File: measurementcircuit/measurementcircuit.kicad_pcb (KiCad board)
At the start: 2 copper layers, 27 parts, among them J1 2601-3110, J10 Conn_01x02, J11 Conn_01x02, J12 Conn_01x02, J2 2604-3106, J3 2604-3102, J4 2604-3102, J5 2604-3102, J6 2604-3102, J7 2604-3102, J8 Conn_01x02, J9 Conn_01x02

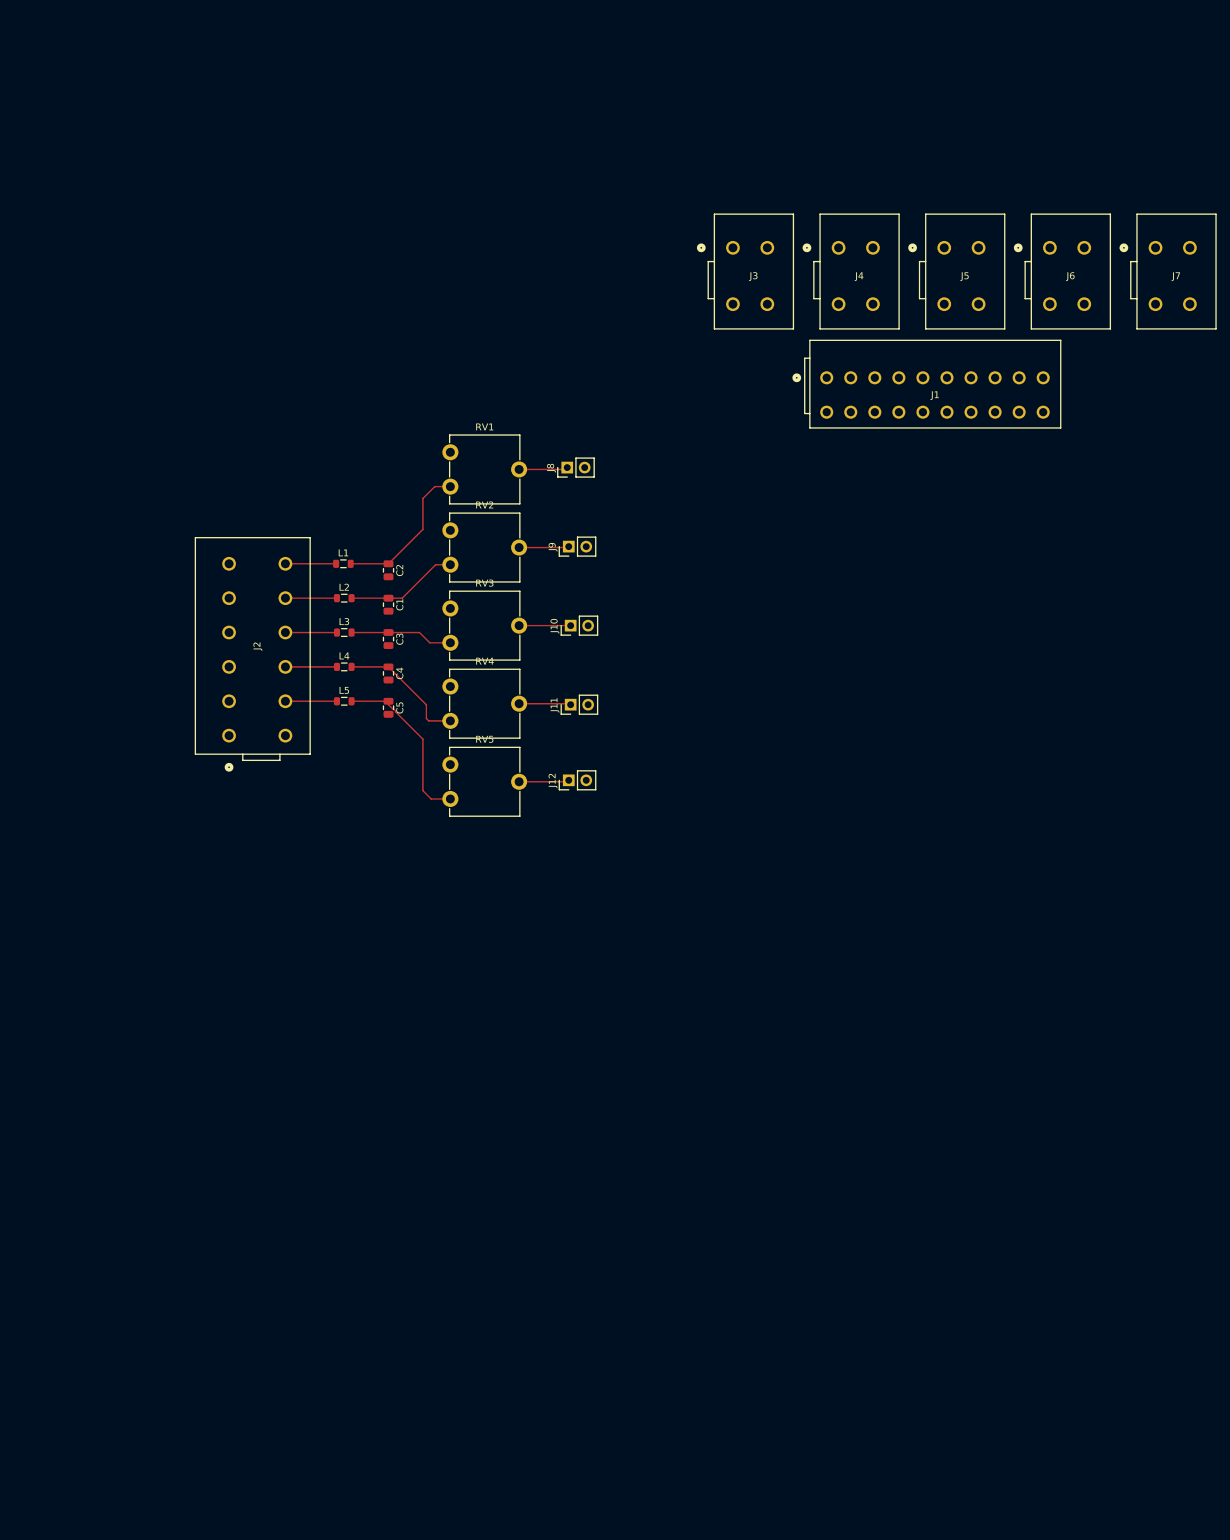
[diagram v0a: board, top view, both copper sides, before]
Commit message: Daniel Measurement Circuit Work
Add more routes to make a total of 8 circuits, component selections and placement, routing, finish schematic and pcb design. Switched back to 3 different circuits with shunts. Just need to fix some issues in the Design Rule Check (DRC) caused by the trace width increase aftor placing routes
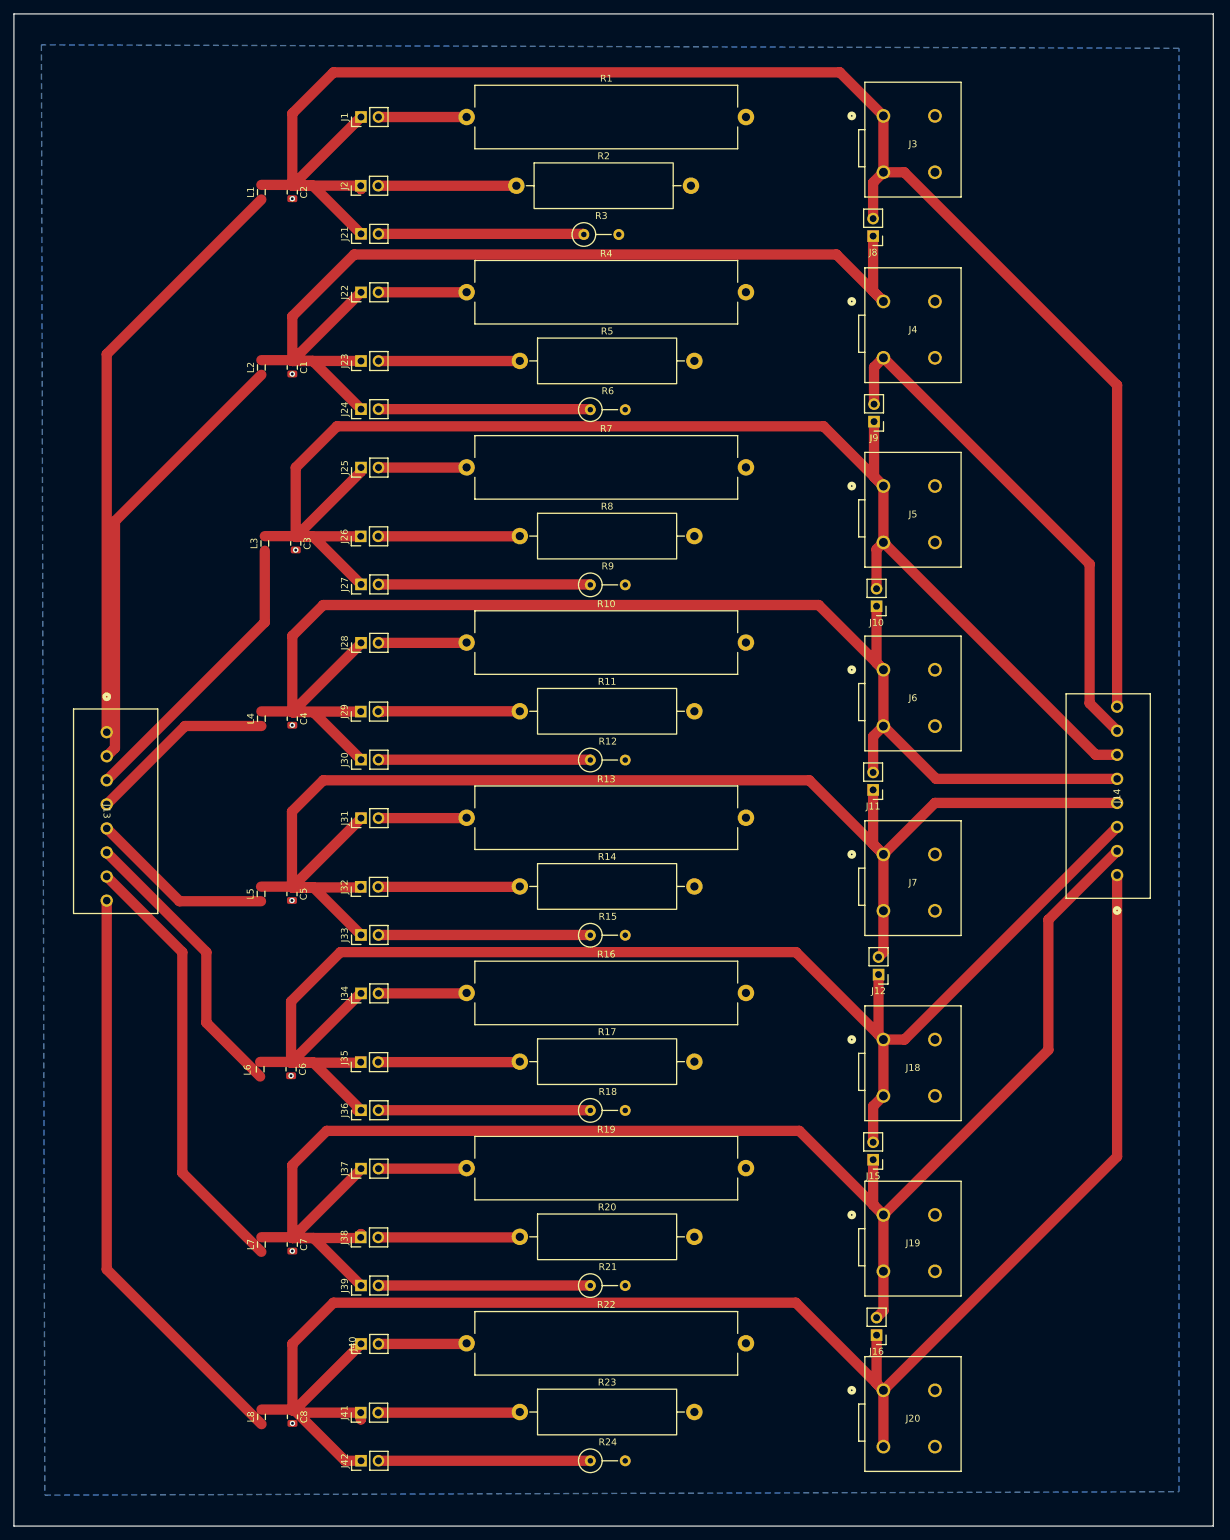
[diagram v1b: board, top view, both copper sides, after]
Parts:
- removed RV1, RV2, RV3, RV4, RV5: 1kΩ, Potentiometer_THT:Potentiometer_ACP_CA9-V10_Vertical
- added C6: 10pF, Capacitor_SMD:C_0805_2012Metric, F.Cu at (50.8, 188.5)
- added C7: 10pF, Capacitor_SMD:C_0805_2012Metric, F.Cu at (51.0, 214.0)
- added C8: 10pF, Capacitor_SMD:C_0805_2012Metric, F.Cu at (51.0, 239.1)
- added J13: 250-108/000-006, WAGO_250-108/000-006_connector_BLUE.pretty:CONN8_250-108&slash_000-006_WAG, F.Cu at (24.0, 139.5)
- added J14: 250-108/000-012, WAGO_250-108/000-012_connector_ORANGE.pretty:CONN8_250-108&slash_000-012_WAG, F.Cu at (171.0, 160.3)
- added J15: Conn_01x02, Connector_PinHeader_2.54mm:PinHeader_1x02_P2.54mm_Vertical, F.Cu at (135.5, 201.7)
- added J16: Conn_01x02, Connector_PinHeader_2.54mm:PinHeader_1x02_P2.54mm_Vertical, F.Cu at (136.0, 227.2)
- added J18: 2604-3102, Wago - 2604-3302_2_pole_connector:CONN2_2604-3302_WAG, F.Cu at (137.0, 184.2)
- added J19: 2604-3102, Wago - 2604-3302_2_pole_connector:CONN2_2604-3302_WAG, F.Cu at (137.0, 209.7)
- added J20: 2604-3102, Wago - 2604-3302_2_pole_connector:CONN2_2604-3302_WAG, F.Cu at (137.0, 235.2)
- added J21: Conn_01x02, Connector_PinHeader_2.54mm:PinHeader_1x02_P2.54mm_Vertical, F.Cu at (61.0, 67.0)
- added J22: Conn_01x02, Connector_PinHeader_2.54mm:PinHeader_1x02_P2.54mm_Vertical, F.Cu at (61.0, 75.5)
- added J23: Conn_01x02, Connector_PinHeader_2.54mm:PinHeader_1x02_P2.54mm_Vertical, F.Cu at (61.0, 85.5)
- added J24: Conn_01x02, Connector_PinHeader_2.54mm:PinHeader_1x02_P2.54mm_Vertical, F.Cu at (61.0, 92.5)
- added J25: Conn_01x02, Connector_PinHeader_2.54mm:PinHeader_1x02_P2.54mm_Vertical, F.Cu at (61.0, 101.0)
- added J26: Conn_01x02, Connector_PinHeader_2.54mm:PinHeader_1x02_P2.54mm_Vertical, F.Cu at (61.0, 111.0)
- added J27: Conn_01x02, Connector_PinHeader_2.54mm:PinHeader_1x02_P2.54mm_Vertical, F.Cu at (61.0, 118.0)
- added J28: Conn_01x02, Connector_PinHeader_2.54mm:PinHeader_1x02_P2.54mm_Vertical, F.Cu at (61.0, 126.5)
- added J29: Conn_01x02, Connector_PinHeader_2.54mm:PinHeader_1x02_P2.54mm_Vertical, F.Cu at (61.0, 136.5)
- added J30: Conn_01x02, Connector_PinHeader_2.54mm:PinHeader_1x02_P2.54mm_Vertical, F.Cu at (61.0, 143.5)
- added J31: Conn_01x02, Connector_PinHeader_2.54mm:PinHeader_1x02_P2.54mm_Vertical, F.Cu at (61.0, 152.0)
- added J32: Conn_01x02, Connector_PinHeader_2.54mm:PinHeader_1x02_P2.54mm_Vertical, F.Cu at (61.0, 162.0)
- added J33: Conn_01x02, Connector_PinHeader_2.54mm:PinHeader_1x02_P2.54mm_Vertical, F.Cu at (61.0, 169.0)
- added J34: Conn_01x02, Connector_PinHeader_2.54mm:PinHeader_1x02_P2.54mm_Vertical, F.Cu at (61.0, 177.5)
- added J35: Conn_01x02, Connector_PinHeader_2.54mm:PinHeader_1x02_P2.54mm_Vertical, F.Cu at (61.0, 187.5)
- added J36: Conn_01x02, Connector_PinHeader_2.54mm:PinHeader_1x02_P2.54mm_Vertical, F.Cu at (61.0, 194.5)
- added J37: Conn_01x02, Connector_PinHeader_2.54mm:PinHeader_1x02_P2.54mm_Vertical, F.Cu at (61.0, 203.0)
- added J38: Conn_01x02, Connector_PinHeader_2.54mm:PinHeader_1x02_P2.54mm_Vertical, F.Cu at (61.0, 213.0)
- added J39: Conn_01x02, Connector_PinHeader_2.54mm:PinHeader_1x02_P2.54mm_Vertical, F.Cu at (61.0, 220.0)
- added J40: Conn_01x02, Connector_PinHeader_2.54mm:PinHeader_1x02_P2.54mm_Vertical, F.Cu at (61.0, 228.5)
- added J41: Conn_01x02, Connector_PinHeader_2.54mm:PinHeader_1x02_P2.54mm_Vertical, F.Cu at (61.0, 238.5)
- added J42: Conn_01x02, Connector_PinHeader_2.54mm:PinHeader_1x02_P2.54mm_Vertical, F.Cu at (61.0, 245.5)
- added L6: 56μH, Inductor_SMD:L_0805_2012Metric, F.Cu at (46.3, 188.5)
- added L7: 56μH, Inductor_SMD:L_0805_2012Metric, F.Cu at (46.5, 214.0)
- added L8: 56μH, Inductor_SMD:L_0805_2012Metric, F.Cu at (46.5, 239.1)
- added R1: 10 Ohm, Resistor_THT:R_Axial_Power_L38.0mm_W9.0mm_P40.64mm, F.Cu at (76.4, 50.0)
- added R10: 10 Ohm, Resistor_THT:R_Axial_Power_L38.0mm_W9.0mm_P40.64mm, F.Cu at (76.4, 126.5)
- added R11: 50 Ohm, Resistor_THT:R_Axial_Power_L20.0mm_W6.4mm_P25.40mm, F.Cu at (84.1, 136.5)
- added R12: 500 Ohm, Resistor_THT:R_Axial_DIN0309_L9.0mm_D3.2mm_P5.08mm_Vertical, F.Cu at (94.4, 143.6)
- added R13: 10 Ohm, Resistor_THT:R_Axial_Power_L38.0mm_W9.0mm_P40.64mm, F.Cu at (76.4, 151.9)
- added R14: 50 Ohm, Resistor_THT:R_Axial_Power_L20.0mm_W6.4mm_P25.40mm, F.Cu at (84.1, 161.9)
- added R15: 500 Ohm, Resistor_THT:R_Axial_DIN0309_L9.0mm_D3.2mm_P5.08mm_Vertical, F.Cu at (94.4, 169.0)
- added R16: 10 Ohm, Resistor_THT:R_Axial_Power_L38.0mm_W9.0mm_P40.64mm, F.Cu at (76.4, 177.4)
- added R17: 50 Ohm, Resistor_THT:R_Axial_Power_L20.0mm_W6.4mm_P25.40mm, F.Cu at (84.1, 187.4)
- added R18: 500 Ohm, Resistor_THT:R_Axial_DIN0309_L9.0mm_D3.2mm_P5.08mm_Vertical, F.Cu at (94.4, 194.5)
- added R19: 10 Ohm, Resistor_THT:R_Axial_Power_L38.0mm_W9.0mm_P40.64mm, F.Cu at (76.4, 202.9)
- added R2: 50 Ohm, Resistor_THT:R_Axial_Power_L20.0mm_W6.4mm_P25.40mm, F.Cu at (83.6, 60.0)
- added R20: 50 Ohm, Resistor_THT:R_Axial_Power_L20.0mm_W6.4mm_P25.40mm, F.Cu at (84.1, 212.9)
- added R21: 500 Ohm, Resistor_THT:R_Axial_DIN0309_L9.0mm_D3.2mm_P5.08mm_Vertical, F.Cu at (94.4, 220.0)
- added R22: 10 Ohm, Resistor_THT:R_Axial_Power_L38.0mm_W9.0mm_P40.64mm, F.Cu at (76.4, 228.4)
- added R23: 50 Ohm, Resistor_THT:R_Axial_Power_L20.0mm_W6.4mm_P25.40mm, F.Cu at (84.1, 238.4)
- added R24: 500 Ohm, Resistor_THT:R_Axial_DIN0309_L9.0mm_D3.2mm_P5.08mm_Vertical, F.Cu at (94.4, 245.5)
- added R3: 500 Ohm, Resistor_THT:R_Axial_DIN0309_L9.0mm_D3.2mm_P5.08mm_Vertical, F.Cu at (93.4, 67.1)
- added R4: 10 Ohm, Resistor_THT:R_Axial_Power_L38.0mm_W9.0mm_P40.64mm, F.Cu at (76.4, 75.5)
- added R5: 50 Ohm, Resistor_THT:R_Axial_Power_L20.0mm_W6.4mm_P25.40mm, F.Cu at (84.1, 85.5)
- added R6: 500 Ohm, Resistor_THT:R_Axial_DIN0309_L9.0mm_D3.2mm_P5.08mm_Vertical, F.Cu at (94.4, 92.6)
- added R7: 10 Ohm, Resistor_THT:R_Axial_Power_L38.0mm_W9.0mm_P40.64mm, F.Cu at (76.4, 101.0)
- added R8: 50 Ohm, Resistor_THT:R_Axial_Power_L20.0mm_W6.4mm_P25.40mm, F.Cu at (84.1, 111.0)
- added R9: 500 Ohm, Resistor_THT:R_Axial_DIN0309_L9.0mm_D3.2mm_P5.08mm_Vertical, F.Cu at (94.4, 118.1)
- J1: value 2601-3110 -> Conn_01x02; footprint Senior_Design:CONN10_2601-3110_WAG -> Connector_PinHeader_2.54mm:PinHeader_1x02_P2.54mm_Vertical
- J2: value 2604-3106 -> Conn_01x02; footprint Senior_Design:CONN6_2604-3106_WAG -> Connector_PinHeader_2.54mm:PinHeader_1x02_P2.54mm_Vertical
- J3, J4, J5, J6, J7: footprint Senior_Design:CONN2_2604-3102_WAG -> Wago - 2604-3302_2_pole_connector:CONN2_2604-3302_WAG
- moved J7 96.7 mm to (137.0, 157.3)
- moved J2 82.3 mm to (61.0, 60.0)
- moved J1 77.6 mm to (61.0, 50.0), turned to 90 degrees
- moved J6 66.0 mm to (137.0, 130.4)
- moved C2 56.8 mm to (51.0, 60.9)
- moved J8 55.8 mm to (135.5, 67.3), turned to 180 degrees
- moved L1 55.4 mm to (46.5, 60.9), turned to 90 degrees
- moved J12 53.2 mm to (136.3, 174.8), turned to 180 degrees
- moved J9 48.0 mm to (135.6, 94.3), turned to 180 degrees
- moved J11 45.7 mm to (135.5, 147.9), turned to 180 degrees
- moved J10 44.6 mm to (136.0, 121.2), turned to 180 degrees
- moved C1 37.2 mm to (51.0, 86.4)
- moved J5 35.8 mm to (137.0, 103.7)
- moved L2 35.7 mm to (46.5, 86.4), turned to 90 degrees
- moved L5 30.5 mm to (46.5, 163.0), turned to 90 degrees
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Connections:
- C1 pad 1: Net-(C1-Pad1) -> Net-(J22-Pin_1)
- C2 pad 1: Net-(C2-Pad1) -> Net-(J1-Pin_1)
- C3 pad 1: Net-(C3-Pad1) -> Net-(J10-Pin_2)
- C4 pad 1: Net-(C4-Pad1) -> Net-(J10-Pin_1)
- C5 pad 1: Net-(C5-Pad1) -> Net-(J11-Pin_1)
- J1 pad 1: Net-(J1-1_1) -> Net-(J1-Pin_1)
- J1 pad 2: Net-(J1-1_1) -> Net-(J1-Pin_2)
- J11 pad 2: Net-(J11-Pin_2) -> Net-(J10-Pin_1)
- J12 pad 2: Net-(J12-Pin_2) -> Net-(J11-Pin_1)
- J2 pad 1: Net-(J2-1_1) -> Net-(J1-Pin_1)
- J2 pad 2: Net-(J2-1_1) -> Net-(J2-Pin_2)
- J3 pad 1: Net-(J3-1_1) -> Net-(J1-Pin_1)
- J3 pad 2: Net-(J3-1_1) -> Net-(J1-Pin_1)
- J3 pad 3: Net-(J1-2_1) -> GND
- J3 pad 4: Net-(J1-1_1) -> GND
- J4 pad 1: Net-(J4-1_1) -> Net-(J22-Pin_1)
- J4 pad 2: Net-(J4-1_1) -> Net-(J22-Pin_1)
- J4 pad 3: Net-(J1-4_1) -> GND
- J4 pad 4: Net-(J1-3_1) -> GND
- J5 pad 3: Net-(J1-6_1) -> GND
- J5 pad 4: Net-(J1-5_1) -> GND
- J6 pad 1: Net-(J11-Pin_2) -> Net-(J10-Pin_1)
- J6 pad 2: Net-(J11-Pin_2) -> Net-(J10-Pin_1)
- J6 pad 3: Net-(J1-8_1) -> GND
- J6 pad 4: Net-(J1-7_1) -> GND
- J7 pad 1: Net-(J12-Pin_2) -> Net-(J11-Pin_1)
- J7 pad 2: Net-(J12-Pin_2) -> Net-(J11-Pin_1)
- J7 pad 3: Net-(J1-10_1) -> GND
- J7 pad 4: Net-(J1-9_1) -> GND
- J8 pad 1: Net-(J8-Pin_1) -> Net-(J22-Pin_1)
- J8 pad 2: Net-(J3-1_1) -> Net-(J1-Pin_1)
- J9 pad 1: Net-(J9-Pin_1) -> Net-(J10-Pin_2)
- J9 pad 2: Net-(J4-1_1) -> Net-(J22-Pin_1)
- L1 pad 1: Net-(J2-6_1) -> Net-(J13-Pad1)
- L1 pad 2: Net-(C2-Pad1) -> Net-(J1-Pin_1)
- L2 pad 1: Net-(J2-5_1) -> Net-(J13-Pad2)
- L2 pad 2: Net-(C1-Pad1) -> Net-(J22-Pin_1)
- L3 pad 1: Net-(J2-4_1) -> Net-(J13-Pad3)
- L3 pad 2: Net-(C3-Pad1) -> Net-(J10-Pin_2)
- L4 pad 1: Net-(J2-3_1) -> Net-(J13-Pad4)
- L4 pad 2: Net-(C4-Pad1) -> Net-(J10-Pin_1)
- L5 pad 1: Net-(J2-2_1) -> Net-(J13-Pad5)
- L5 pad 2: Net-(C5-Pad1) -> Net-(J11-Pin_1)
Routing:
- net Net-(J1-Pin_1): track 0.00 -> 252.8 mm
- net Net-(J16-Pin_1): track 0.00 -> 251.4 mm
- net Net-(J15-Pin_1): track 0.00 -> 236.9 mm
- net Net-(J22-Pin_1): track 0.00 -> 226.4 mm
- net Net-(J10-Pin_2): track 0.00 -> 214.3 mm
- net Net-(J12-Pin_1): track 7.31 -> 218.2 mm
- net Net-(J11-Pin_1): track 7.56 -> 207.5 mm
- net Net-(J10-Pin_1): track 7.50 -> 206.9 mm
- net Net-(J13-Pad1): track 0.00 -> 86.8 mm
- net Net-(J13-Pad8): track 0.00 -> 85.5 mm
- net Net-(J13-Pad2): track 0.00 -> 64.8 mm
- net Net-(J13-Pad7): track 0.00 -> 63.9 mm
- net Net-(J13-Pad3): track 0.00 -> 42.9 mm
- net Net-(J13-Pad6): track 0.00 -> 41.8 mm
- net Net-(J24-Pin_2): track 0.00 -> 30.9 mm
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- added copper zone on B.Cu, net GND
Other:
- board outline added: 174.5 x 220 mm

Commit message: Update
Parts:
- removed J14: 250-108/000-012, WAGO_250-108/000-012_connector_ORANGE.pretty:CONN8_250-108&slash_000-012_WAG
- added J17: 250-116/000-012, Senior_Design:CONN16_250-116&slash_000-012_WAG, F.Cu at (-13.5, -5.50)
- moved C5 235.4 mm to (-154.8, 48.8)
- moved C6 235.4 mm to (-155.0, 74.3)
- moved L5 235.4 mm to (-159.3, 48.8)
- moved L6 235.4 mm to (-159.5, 74.3)
- moved R1 235.4 mm to (-129.4, -64.2)
- moved R10 235.4 mm to (-129.4, 12.2)
- moved R13 235.4 mm to (-129.4, 37.7)
- moved R16 235.4 mm to (-129.4, 63.2)
- moved R19 235.4 mm to (-129.4, 88.7)
- moved R22 235.4 mm to (-129.4, 114.2)
- moved R3 235.4 mm to (-112.4, -47.1)
- moved R4 235.4 mm to (-129.4, -38.7)
- moved R7 235.4 mm to (-129.4, -13.2)
- moved C1 235.4 mm to (-154.8, -27.8)
- moved C2 235.4 mm to (-154.8, -53.3)
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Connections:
- C2 pad 1: Net-(J1-Pin_1) -> Net-(C2-Pad1)
- C3 pad 1: Net-(J10-Pin_2) -> Net-(C3-Pad1)
- C5 pad 1: Net-(J11-Pin_1) -> Net-(C5-Pad1)
- C6 pad 1: Net-(J12-Pin_1) -> Net-(C6-Pad1)
- C7 pad 1: Net-(J15-Pin_1) -> Net-(C7-Pad1)
- C8 pad 1: Net-(J16-Pin_1) -> Net-(C8-Pad1)
- J18 pad 3: GND -> Net-(J18-2_1)
- J18 pad 4: GND -> Net-(J18-2_1)
- J19 pad 3: GND -> Net-(J19-2_1)
- J19 pad 4: GND -> Net-(J19-2_1)
- J20 pad 3: GND -> Net-(J20-2_1)
- J20 pad 4: GND -> Net-(J20-2_1)
- J3 pad 3: GND -> Net-(J3-2_1)
- J3 pad 4: GND -> Net-(J3-2_1)
- J4 pad 3: GND -> Net-(J4-2_1)
- J4 pad 4: GND -> Net-(J4-2_1)
- J5 pad 3: GND -> Net-(J5-2_1)
- J5 pad 4: GND -> Net-(J5-2_1)
- J6 pad 3: GND -> Net-(J6-2_1)
- J6 pad 4: GND -> Net-(J6-2_1)
- J7 pad 3: GND -> Net-(J7-2_1)
- J7 pad 4: GND -> Net-(J7-2_1)
- L1 pad 2: Net-(J1-Pin_1) -> Net-(C2-Pad1)
- L3 pad 2: Net-(J10-Pin_2) -> Net-(C3-Pad1)
- L5 pad 2: Net-(J11-Pin_1) -> Net-(C5-Pad1)
- L6 pad 2: Net-(J12-Pin_1) -> Net-(C6-Pad1)
- L7 pad 2: Net-(J15-Pin_1) -> Net-(C7-Pad1)
- L8 pad 2: Net-(J16-Pin_1) -> Net-(C8-Pad1)
- R1 pad 2: GND -> Net-(C2-Pad1)
- R10 pad 2: GND -> Net-(J10-Pin_1)
- R11 pad 2: GND -> Net-(J10-Pin_1)
- R12 pad 2: GND -> Net-(J10-Pin_1)
- R13 pad 2: GND -> Net-(C5-Pad1)
- R14 pad 2: GND -> Net-(C5-Pad1)
- R15 pad 2: GND -> Net-(C5-Pad1)
- R16 pad 2: GND -> Net-(C6-Pad1)
- R17 pad 2: GND -> Net-(C6-Pad1)
- R18 pad 2: GND -> Net-(C6-Pad1)
- R19 pad 2: GND -> Net-(C7-Pad1)
- R2 pad 2: GND -> Net-(C2-Pad1)
- R20 pad 2: GND -> Net-(C7-Pad1)
- R21 pad 2: GND -> Net-(C7-Pad1)
- R22 pad 2: GND -> Net-(C8-Pad1)
- R23 pad 2: GND -> Net-(C8-Pad1)
- R24 pad 2: GND -> Net-(C8-Pad1)
- R3 pad 2: GND -> Net-(C2-Pad1)
- R4 pad 2: GND -> Net-(J22-Pin_1)
- R5 pad 2: GND -> Net-(J22-Pin_1)
- R6 pad 2: GND -> Net-(J22-Pin_1)
- R7 pad 2: GND -> Net-(C3-Pad1)
- R8 pad 2: GND -> Net-(C3-Pad1)
- R9 pad 2: GND -> Net-(C3-Pad1)
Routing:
- net Net-(J22-Pin_1): vias 0 -> 3
- net Net-(J7-2_1): vias 0 -> 2
- net Net-(J6-2_1): vias 0 -> 2
- net Net-(J5-2_1): vias 0 -> 2
- net Net-(J4-2_1): vias 0 -> 2
- net Net-(J3-2_1): vias 0 -> 2
- net Net-(J20-2_1): vias 0 -> 2
- net Net-(J19-2_1): vias 0 -> 2
- net Net-(J18-2_1): vias 0 -> 2
- net Net-(J10-Pin_1): vias 0 -> 3
- net Net-(C8-Pad1): vias 0 -> 3
- net Net-(C7-Pad1): vias 0 -> 3
- net Net-(C6-Pad1): vias 0 -> 3
- net Net-(C5-Pad1): vias 0 -> 3
- net Net-(C3-Pad1): vias 0 -> 3
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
